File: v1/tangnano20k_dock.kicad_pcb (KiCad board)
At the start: 2 copper layers, 161.9 x 73.7 mm, 80 parts, among them J1 Mini-DIN-6, J10 DB9_Male_MountingHoles, J11 DB9_Male_MountingHoles, J2 2x20 Pin Female, J3 Conn_01x03_Male, J4 Conn_01x20, J5 Conn_01x02, J6 RCA, J7 FCR684205T, J8 AudioJack3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

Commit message: Drive PiTube PHI2 from WS2812 output, freeing up PWM
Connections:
- J2 pad 26: /PWM_R -> /PHI2
- J2 pad 40: /PWM_L -> unconnected-(J2-Pad40)
- J4 pad 2: GND -> /PWM_L
- J4 pad 3: /PWM_L -> /PWM_R
- J4 pad 4: /PWM_R -> /VGA_HS
- J4 pad 5: /VGA_HS -> /PHI2
- U2 pad 27: unconnected-(U2-Pad27) -> /PHI2
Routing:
- net /PHI2: track 0.00 -> 115.5 mm
- net /PWM_L: track 126.3 -> 36.4 mm, vias 1 -> 0
- net /PWM_R: track 107.8 -> 36.9 mm
- net /VGA_HS: track 17.0 -> 19.9 mm
- net /SPDIF: track 57.8 -> 60.7 mm
- net /KBD_CONFIG_MODIFIER: track 38.1 -> 35.6 mm
- net /JS_Load_n: track 138.6 -> 140.7 mm
- net /JS_Data: track 41.1 -> 42.8 mm
- net /JS_Clk: track 133.0 -> 134.1 mm

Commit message: Correct swapped net names LED3 and LED5
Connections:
- J2 pad 3: /LED5 -> /LED3
- J2 pad 7: /LED3 -> /LED5
- J4 pad 16: /LED3 -> /LED5
- J4 pad 18: /LED5 -> /LED3
- U2 pad 16: /LED3 -> /LED5
- U2 pad 18: /LED5 -> /LED3
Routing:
- net /LED5: track 93.9 -> 95.0 mm
- net /LED3: track 95.0 -> 93.9 mm
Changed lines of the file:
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@@
       (net 135 "Net-(J2-Pad2)") (pinfunction "Pin_2") (pintype "passive"))
     (pad "3" thru_hole oval (at 0 2.54) (size 1.7 1.7) (drill 1) (layers *.Cu *.Mask)
-      (net 51 "/LED5") (pinfunction "Pin_3") (pintype "passive"))
+      (net 36 "/LED3") (pinfunction "Pin_3") (pintype "passive"))
     (pad "4" thru_hole oval (at -2.54 2.54) (size 1.7 1.7) (drill 1) (layers *.Cu *.Mask)
       (net 135 "Net-(J2-Pad2)") (pinfunction "Pin_4") (pintype "passive"))
@@
       (net 1 "GND") (pinfunction "Pin_6") (pintype "passive"))
     (pad "7" thru_hole oval (at 0 7.62) (size 1.7 1.7) (drill 1) (layers *.Cu *.Mask)
-      (net 36 "/LED3") (pinfunction "Pin_7") (pintype "passive"))
+      (net 51 "/LED5") (pinfunction "Pin_7") (pintype "passive"))
     (pad "8" thru_hole oval (at -2.54 7.62) (size 1.7 1.7) (drill 1) (layers *.Cu *.Mask)
       (net 33 "/SerialTx") (pinfunction "Pin_8") (pintype "passive"))
@@
       (net 31 "/LED2") (pinfunction "Pin17_LED2") (pintype "passive"))
     (pad "16" thru_hole circle (at 0 38.1 180) (size 1.524 1.524) (drill 0.762) (layers *.Cu *.Mask)
-      (net 36 "/LED3") (pinfunction "Pin20_LED5") (pintype "passive"))
+      (net 51 "/LED5") (pinfunction "Pin20_LED5") (pintype "passive"))
     (pad "17" thru_hole circle (at 0 40.64 180) (size 1.524 1.524) (drill 0.762) (layers *.Cu *.Mask)
       (net 35 "/LED4") (pinfunction "Pin19_LED4") (pintype "passive"))
     (pad "18" thru_hole circle (at 0 43.18 180) (size 1.524 1.524) (drill 0.762) (layers *.Cu *.Mask)
-      (net 51 "/LED5") (pinfunction "Pin18_LED3") (pintype "passive"))
+      (net 36 "/LED3") (pinfunction "Pin18_LED3") (pintype "passive"))
     (pad "19" thru_hole circle (at 0 45.72 180) (size 1.524 1.524) (drill 0.762) (layers *.Cu *.Mask)
       (net 3 "+3.3V") (pinfunction "3V3") (pintype "passive"))
@@
       (net 31 "/LED2") (pinfunction "Pin_15") (pintype "passive"))
     (pad "16" thru_hole oval (at 0 38.1 180) (size 1.7 1.7) (drill 1) (layers *.Cu *.Mask)
-      (net 36 "/LED3") (pinfunction "Pin_16") (pintype "passive"))
+      (net 51 "/LED5") (pinfunction "Pin_16") (pintype "passive"))
     (pad "17" thru_hole oval (at 0 40.64 180) (size 1.7 1.7) (drill 1) (layers *.Cu *.Mask)
       (net 35 "/LED4") (pinfunction "Pin_17") (pintype "passive"))
     (pad "18" thru_hole oval (at 0 43.18 180) (size 1.7 1.7) (drill 1) (layers *.Cu *.Mask)
-      (net 51 "/LED5") (pinfunction "Pin_18") (pintype "passive"))
+      (net 36 "/LED3") (pinfunction "Pin_18") (pintype "passive"))
     (pad "19" thru_hole oval (at 0 45.72 180) (size 1.7 1.7) (drill 1) (layers *.Cu *.Mask)
       (net 1 "GND") (pinfunction "Pin_19") (pintype "passive"))
@@
   (segment (start 165.105 53.97) (end 185.42 53.97) (width 0.254) (layer "F.Cu") (net 35))
   (segment (start 198.12 66.67) (end 198.12 67.94) (width 0.254) (layer "F.Cu") (net 35))
-  (segment (start 184.785 54.605) (end 196.85 66.67) (width 0.254) (layer "F.Cu") (net 36))
-  (segment (start 161.295 64.765) (end 163.195 62.865) (width 0.254) (layer "F.Cu") (net 36))
-  (segment (start 138.43 64.135) (end 139.06 64.765) (width 0.254) (layer "F.Cu") (net 36))
-  (segment (start 196.85 66.67) (end 196.85 68.575) (width 0.254) (layer "F.Cu") (net 36))
-  (segment (start 199.39 71.115) (end 208.28 71.115) (width 0.254) (layer "F.Cu") (net 36))
-  (segment (start 135.89 64.135) (end 130.81 64.135) (width 0.254) (layer "F.Cu") (net 36))
-  (segment (start 163.195 62.865) (end 163.195 57.15) (width 0.254) (layer "F.Cu") (net 36))
-  (segment (start 163.195 57.15) (end 165.74 54.605) (width 0.254) (layer "F.Cu") (net 36))
-  (segment (start 208.28 71.115) (end 209.55 69.845) (width 0.254) (layer "F.Cu") (net 36))
-  (segment (start 165.74 54.605) (end 184.785 54.605) (width 0.254) (layer "F.Cu") (net 36))
-  (segment (start 139.06 64.765) (end 161.295 64.765) (width 0.254) (layer "F.Cu") (net 36))
-  (segment (start 137.805 64.135) (end 138.43 64.135) (width 0.254) (layer "F.Cu") (net 36))
-  (segment (start 196.85 68.575) (end 199.39 71.115) (width 0.254) (layer "F.Cu") (net 36))
-  (segment (start 135.89 64.13) (end 137.8 64.13) (width 0.254) (layer "F.Cu") (net 36))
-  (segment (start 137.8 64.13) (end 137.805 64.135) (width 0.254) (layer "F.Cu") (net 36))
+  (segment (start 161.925 61.595) (end 160.025 63.495) (width 0.254) (layer "F.Cu") (net 36))
+  (segment (start 164.47 53.335) (end 161.925 55.88) (width 0.254) (layer "F.Cu") (net 36))
+  (segment (start 135.89 59.055) (end 130.81 59.055) (width 0.254) (layer "F.Cu") (net 36))
+  (segment (start 141.6 63.495) (end 137.16 59.055) (width 0.254) (layer "F.Cu") (net 36))
+  (segment (start 160.025 63.495) (end 141.6 63.495) (width 0.254) (layer "F.Cu") (net 36))
+  (segment (start 137.16 59.055) (end 135.895 59.055) (width 0.254) (layer "F.Cu") (net 36))
+  (segment (start 208.28 66.035) (end 198.755 66.035) (width 0.254) (layer "F.Cu") (net 36))
+  (segment (start 198.755 66.035) (end 186.055 53.335) (width 0.254) (layer "F.Cu") (net 36))
+  (segment (start 209.55 64.765) (end 208.28 66.035) (width 0.254) (layer "F.Cu") (net 36))
+  (segment (start 186.055 53.335) (end 164.47 53.335) (width 0.254) (layer "F.Cu") (net 36))
+  (segment (start 161.925 55.88) (end 161.925 61.595) (width 0.254) (layer "F.Cu") (net 36))
   (segment (start 196.85 74.29) (end 198.755 76.195) (width 0.254) (layer "F.Cu") (net 37))
   (segment (start 138.43 90.165) (end 137.795 89.53) (width 0.254) (layer "F.Cu") (net 37))
@@
   (segment (start 95.885 102.865) (end 95.885 100.895) (width 0.254) (layer "F.Cu") (net 50))
   (segment (start 96.52 104.49) (end 96.52 103.5) (width 0.254) (layer "F.Cu") (net 50))
-  (segment (start 161.925 61.595) (end 160.025 63.495) (width 0.254) (layer "F.Cu") (net 51))
-  (segment (start 164.47 53.335) (end 161.925 55.88) (width 0.254) (layer "F.Cu") (net 51))
-  (segment (start 135.89 59.055) (end 130.81 59.055) (width 0.254) (layer "F.Cu") (net 51))
-  (segment (start 141.6 63.495) (end 137.16 59.055) (width 0.254) (layer "F.Cu") (net 51))
-  (segment (start 160.025 63.495) (end 141.6 63.495) (width 0.254) (layer "F.Cu") (net 51))
-  (segment (start 137.16 59.055) (end 135.895 59.055) (width 0.254) (layer "F.Cu") (net 51))
-  (segment (start 208.28 66.035) (end 198.755 66.035) (width 0.254) (layer "F.Cu") (net 51))
-  (segment (start 198.755 66.035) (end 186.055 53.335) (width 0.254) (layer "F.Cu") (net 51))
-  (segment (start 209.55 64.765) (end 208.28 66.035) (width 0.254) (layer "F.Cu") (net 51))
-  (segment (start 186.055 53.335) (end 164.47 53.335) (width 0.254) (layer "F.Cu") (net 51))
-  (segment (start 161.925 55.88) (end 161.925 61.595) (width 0.254) (layer "F.Cu") (net 51))
+  (segment (start 184.785 54.605) (end 196.85 66.67) (width 0.254) (layer "F.Cu") (net 51))
+  (segment (start 161.295 64.765) (end 163.195 62.865) (width 0.254) (layer "F.Cu") (net 51))
+  (segment (start 138.43 64.135) (end 139.06 64.765) (width 0.254) (layer "F.Cu") (net 51))
+  (segment (start 196.85 66.67) (end 196.85 68.575) (width 0.254) (layer "F.Cu") (net 51))
+  (segment (start 199.39 71.115) (end 208.28 71.115) (width 0.254) (layer "F.Cu") (net 51))
+  (segment (start 135.89 64.135) (end 130.81 64.135) (width 0.254) (layer "F.Cu") (net 51))
+  (segment (start 163.195 62.865) (end 163.195 57.15) (width 0.254) (layer "F.Cu") (net 51))
+  (segment (start 163.195 57.15) (end 165.74 54.605) (width 0.254) (layer "F.Cu") (net 51))
+  (segment (start 208.28 71.115) (end 209.55 69.845) (width 0.254) (layer "F.Cu") (net 51))
+  (segment (start 165.74 54.605) (end 184.785 54.605) (width 0.254) (layer "F.Cu") (net 51))
+  (segment (start 139.06 64.765) (end 161.295 64.765) (width 0.254) (layer "F.Cu") (net 51))
+  (segment (start 137.805 64.135) (end 138.43 64.135) (width 0.254) (layer "F.Cu") (net 51))
+  (segment (start 196.85 68.575) (end 199.39 71.115) (width 0.254) (layer "F.Cu") (net 51))
+  (segment (start 135.89 64.13) (end 137.8 64.13) (width 0.254) (layer "F.Cu") (net 51))
+  (segment (start 137.8 64.13) (end 137.805 64.135) (width 0.254) (layer "F.Cu") (net 51))
   (segment (start 106.6775 92.705) (end 106.0475 92.705) (width 0.254) (layer "F.Cu") (net 52))
   (segment (start 110.49 94.615) (end 108.5875 94.615) (width 0.254) (layer "F.Cu") (net 52))

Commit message: Add KEY_CONF to DEBUG header
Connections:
- J4 pad 19: GND -> /KEY_CONF
- J5 pad 1: /KBD_CONFIG_MODIFIER -> /KEY_CONF
- U2 pad 3: /KBD_CONFIG_MODIFIER -> /KEY_CONF
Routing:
- net /KEY_CONF: track 0.00 -> 83.9 mm, vias 0 -> 3
- net /KBD_CONFIG_MODIFIER: track 35.6 -> 0.00 mm, vias 2 -> 0
- net /JS_Clk: track 134.1 -> 130.4 mm
- net /JS_Load_n: track 140.7 -> 137.8 mm

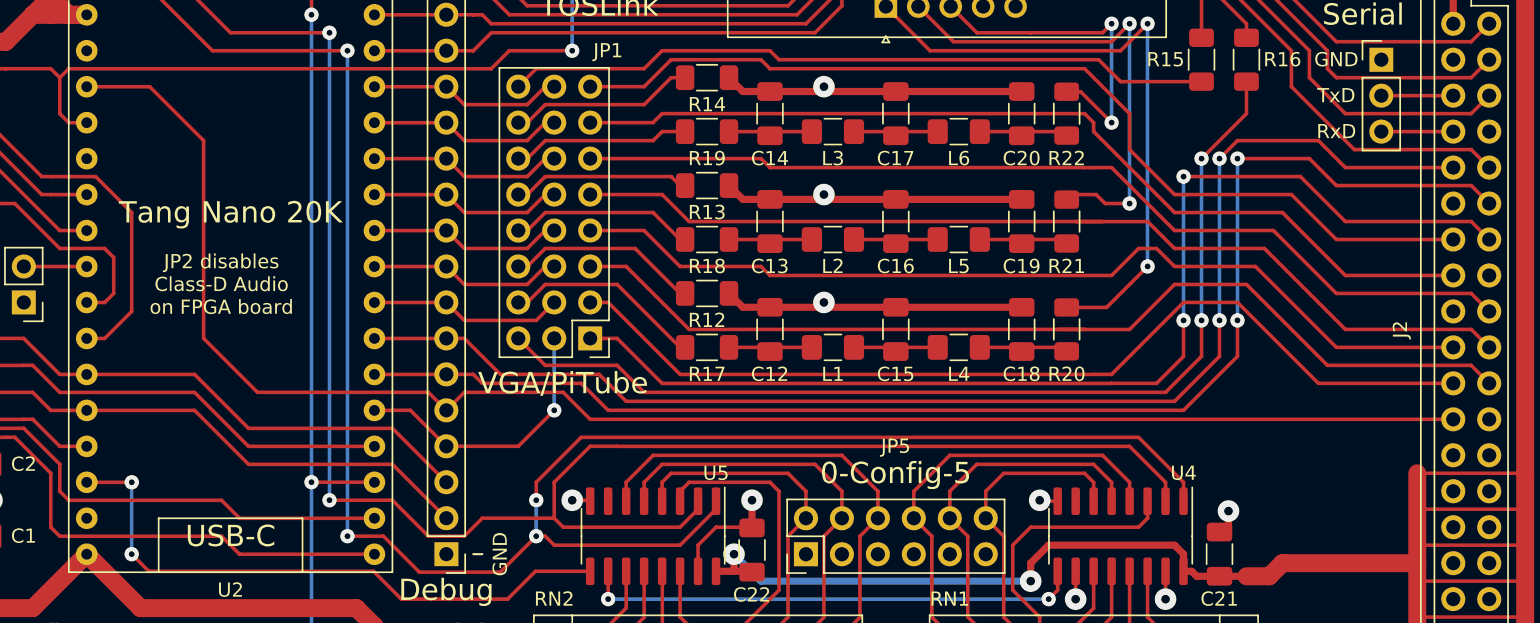
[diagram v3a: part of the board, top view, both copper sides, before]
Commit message: Drive PiTube PHI2 from js_clk to save a pin
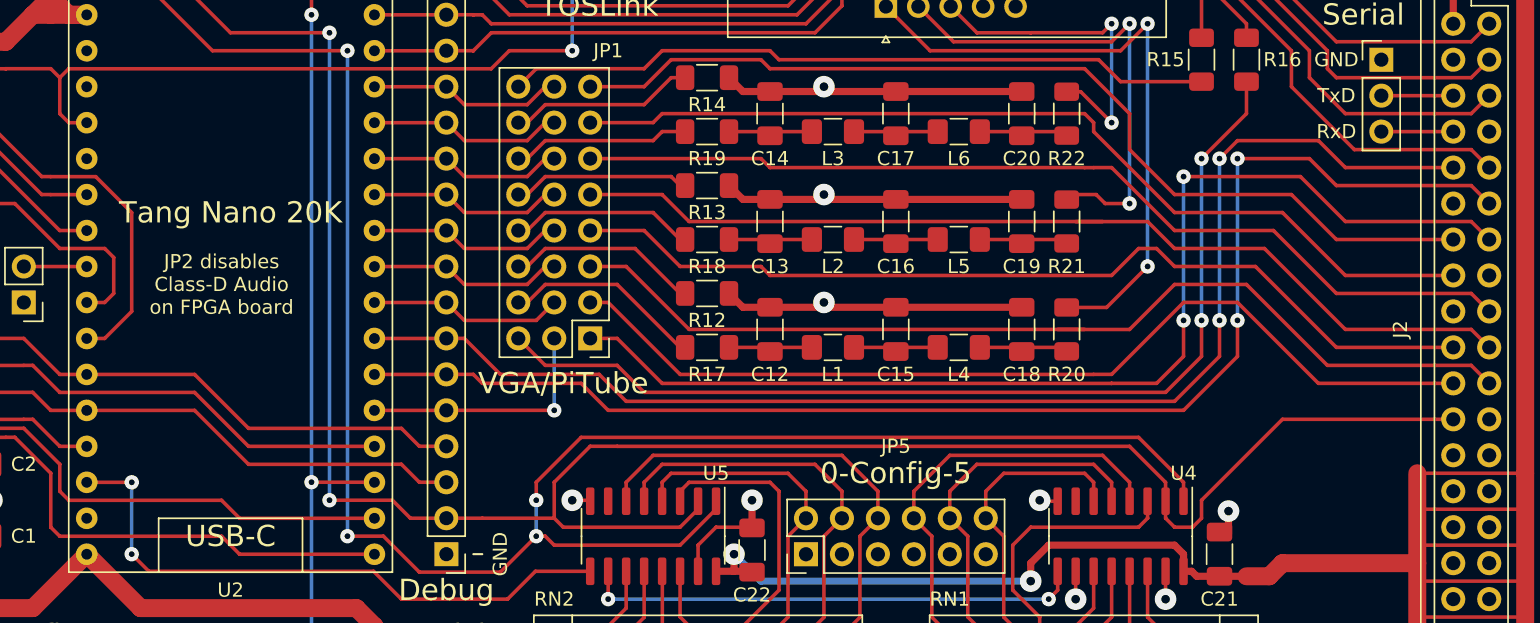
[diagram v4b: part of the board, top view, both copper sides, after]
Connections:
- J4 pad 2: /PWM_L -> /PHI2
- J4 pad 3: /PWM_R -> /PWM_L
- J4 pad 4: /VGA_HS -> /PWM_R
- J4 pad 5: /PHI2 -> /VGA_HS
- U2 pad 23: /JS_Clk -> /PHI2
- U2 pad 27: /PHI2 -> unconnected-(U2-Pad27)
- U4 pad 2: /JS_Clk -> /PHI2
- U5 pad 2: /JS_Clk -> /PHI2
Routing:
- net /JS_Clk: track 130.4 -> 0.00 mm, vias 2 -> 0
- net /PHI2: track 115.5 -> 155.0 mm, vias 0 -> 2
- net /VGA_HS: track 19.9 -> 17.8 mm
- net /PWM_R: track 36.9 -> 35.9 mm
- net /PWM_L: track 36.4 -> 35.4 mm

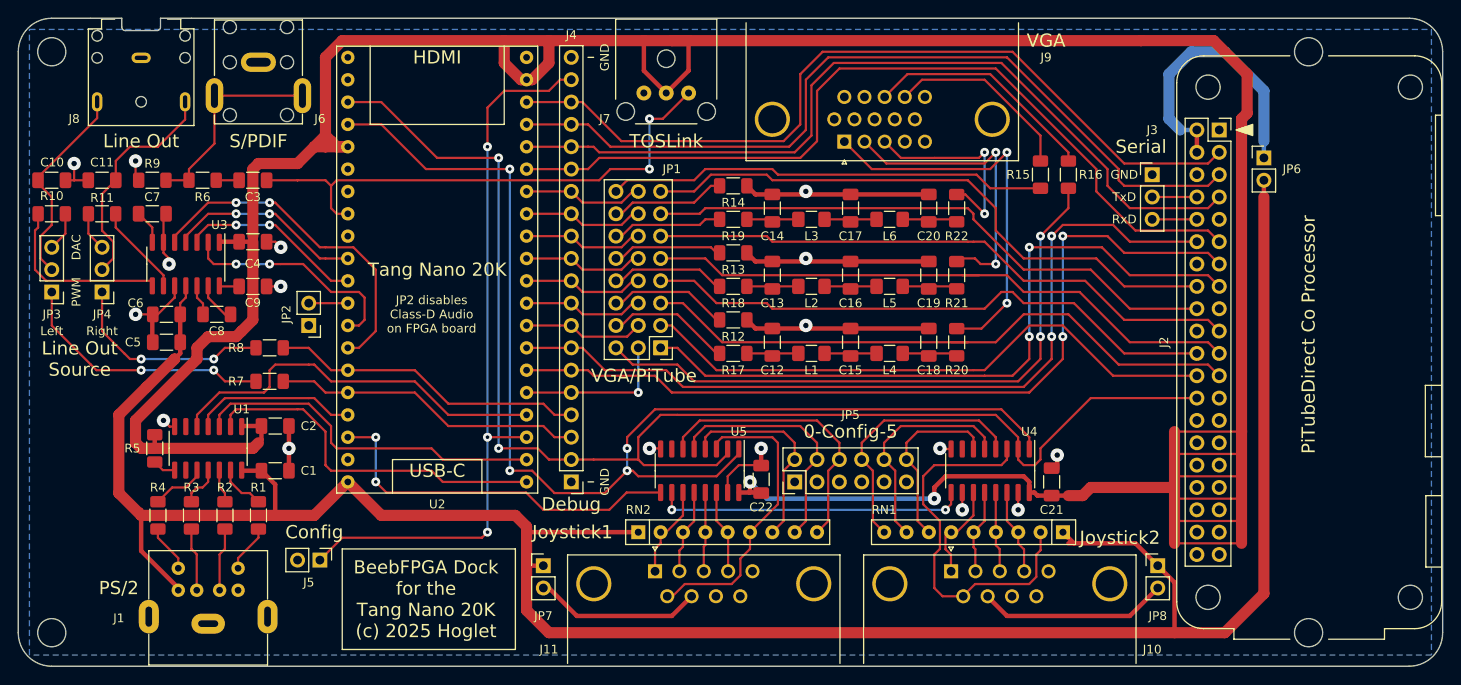
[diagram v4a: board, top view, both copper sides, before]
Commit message: Add an RC filter to allow PHI2 clock edge to be slowed to avoid ringing
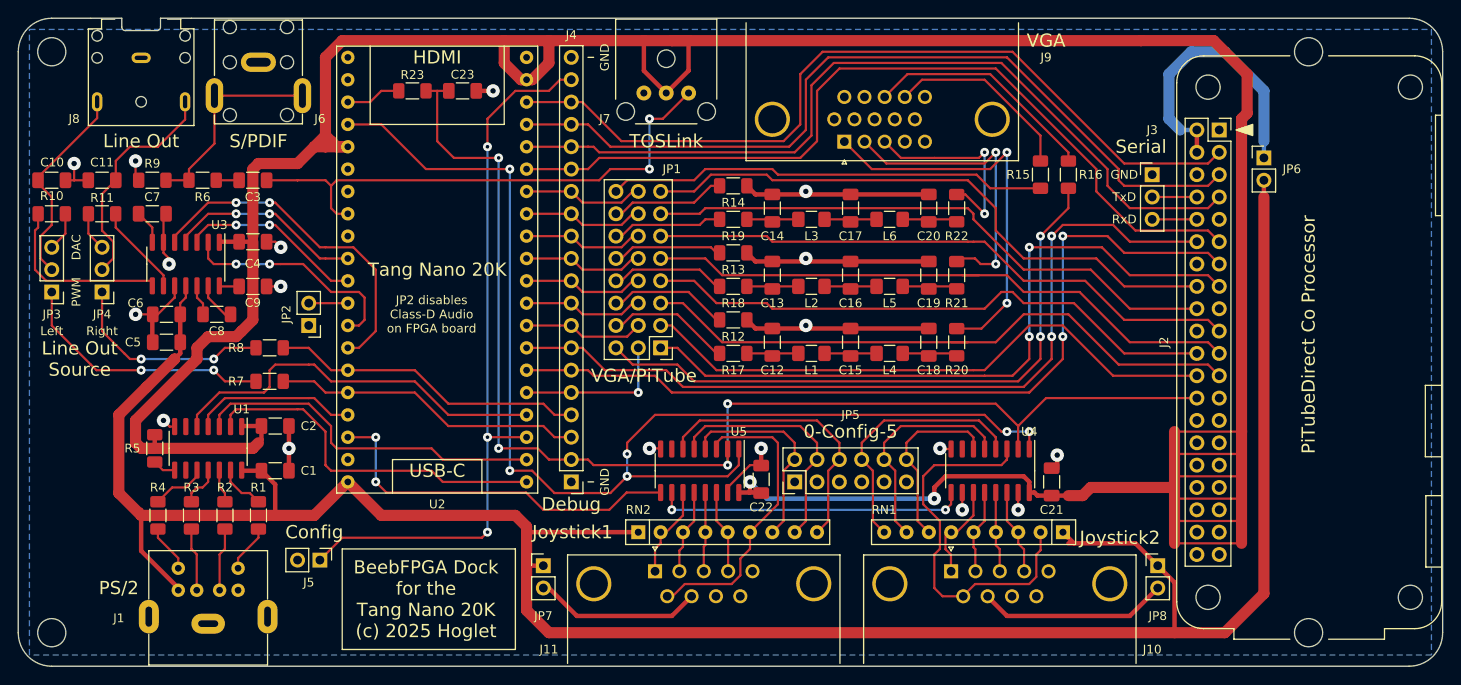
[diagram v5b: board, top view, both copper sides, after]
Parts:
- added C23: 47p, Capacitor_SMD:C_1206_3216Metric_Pad1.33x1.80mm_HandSolder, F.Cu at (123.5, 57.8)
- added R23: 120R, Resistor_SMD:R_1206_3216Metric_Pad1.30x1.75mm_HandSolder, F.Cu at (117.8, 57.8)
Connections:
- U2 pad 23: /PHI2 -> Net-(R23-Pad1)
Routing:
- net /PHI2: track 155.0 -> 143.1 mm, vias 2 -> 4
- net Net-(R23-Pad1): track 0.00 -> 6.32 mm
- net /KEY_CONF: track 83.9 -> 83.2 mm
- net GND: track 112.8 -> 113.4 mm, vias 17 -> 18
- net /JS_Load_n: track 137.8 -> 138.1 mm, vias 4 -> 6

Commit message: Added Cliff DC10A power jack + schottky diode
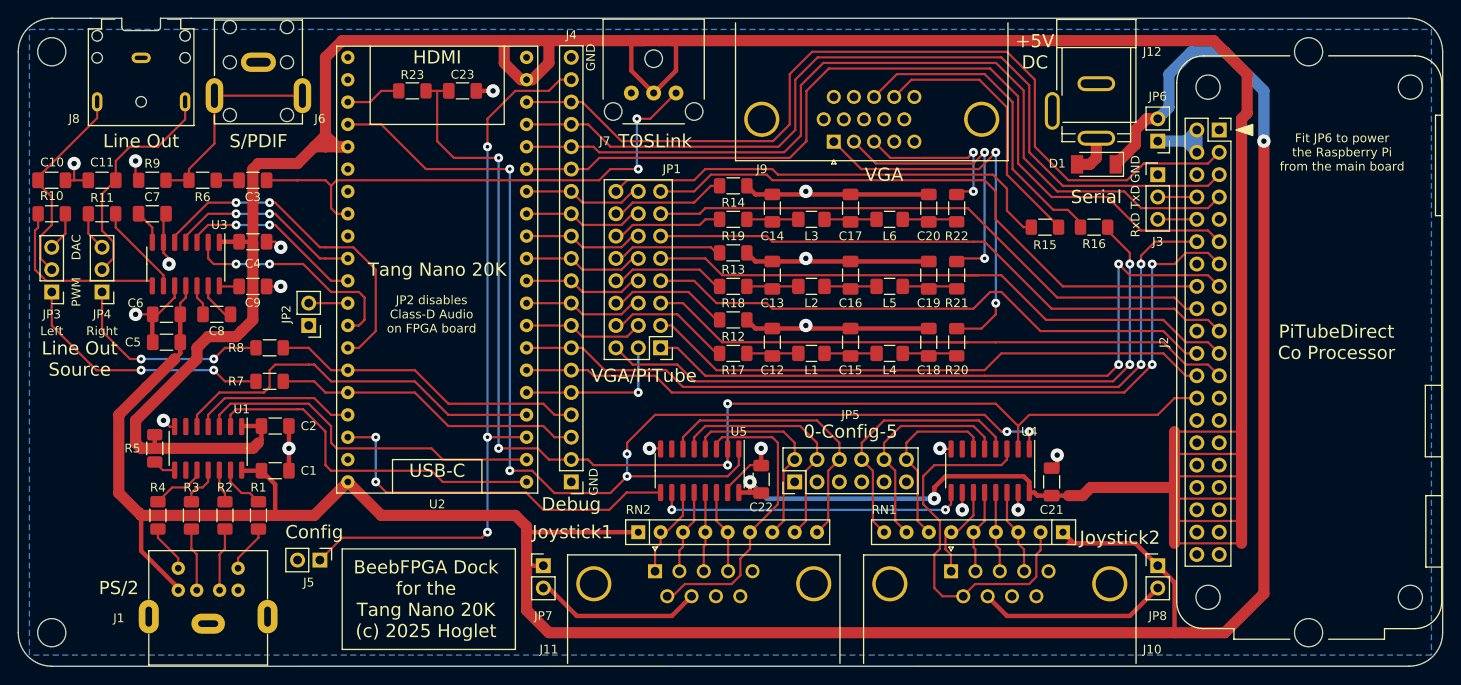
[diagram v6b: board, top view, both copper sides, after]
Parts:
- added D1: PMEG3020EP, Diode_SMD:D_SOD-128, F.Cu at (195.6, 66.1)
- added J12: Cliff DC10A, TangNano20k:CLIFF_FC68148_DC10A, F.Cu at (195.6, 49.5)
- moved JP6 12.2 mm to (202.6, 63.5), turned to 180 degrees
- moved R16 6.65 mm to (195.3, 73.3), turned to 180 degrees
- moved R15 5.99 mm to (189.7, 73.3), turned to 0 degrees
- moved J7 1.43 mm to (145.3, 49.5)
- moved J9 1.20 mm to (165.7, 63.5)
- moved J3 0.63 mm to (202.6, 67.3)
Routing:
- net +5V: track 275.7 -> 313.0 mm, vias 0 -> 1
- net Net-(J2-Pad2): track 32.6 -> 9.31 mm
- net Net-(J9-Pad13): track 26.6 -> 36.0 mm
- net Net-(J9-Pad14): track 21.8 -> 30.9 mm
- net /LED3: track 93.9 -> 99.9 mm
- net /VGA/VGA_HS: track 71.6 -> 77.0 mm
- net Net-(J9-Pad3): track 23.4 -> 18.3 mm
- net Net-(D1-Pad2): track 0.00 -> 4.73 mm
- net /LED4: track 94.7 -> 98.3 mm
- net /LED5: track 95.0 -> 98.3 mm
- net /LED0: track 96.7 -> 93.6 mm
- net /LED2: track 96.5 -> 99.4 mm
- net /DATA3: track 71.5 -> 68.8 mm
- net /DATA0: track 67.5 -> 64.9 mm
- net /LED1: track 94.6 -> 92.1 mm
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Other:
- board text added: "+5V DC"
- board text added: "Fit JP6 to power the Raspberry Pi from the main board"
